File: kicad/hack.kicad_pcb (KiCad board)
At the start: 2 copper layers, 33.5 x 23.4 mm, 33 parts, among them P1 USB_micro, P2 CONN_01X13, P3 CONN_01X13, P4 CONN_01X01, U1 MIC5528, U2 STF202, U3 ATSAMD21E, X1 MC-306

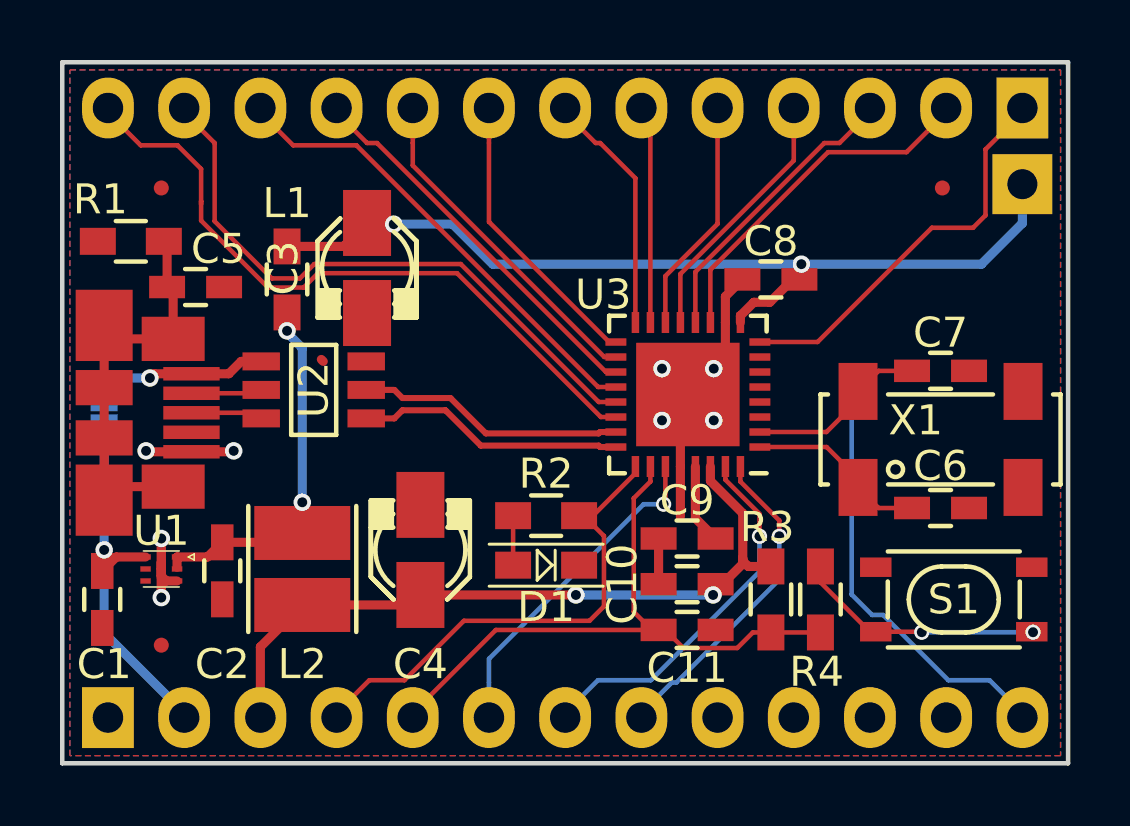
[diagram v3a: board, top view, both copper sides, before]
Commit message: Layout 100% completed, cosmetics not yet
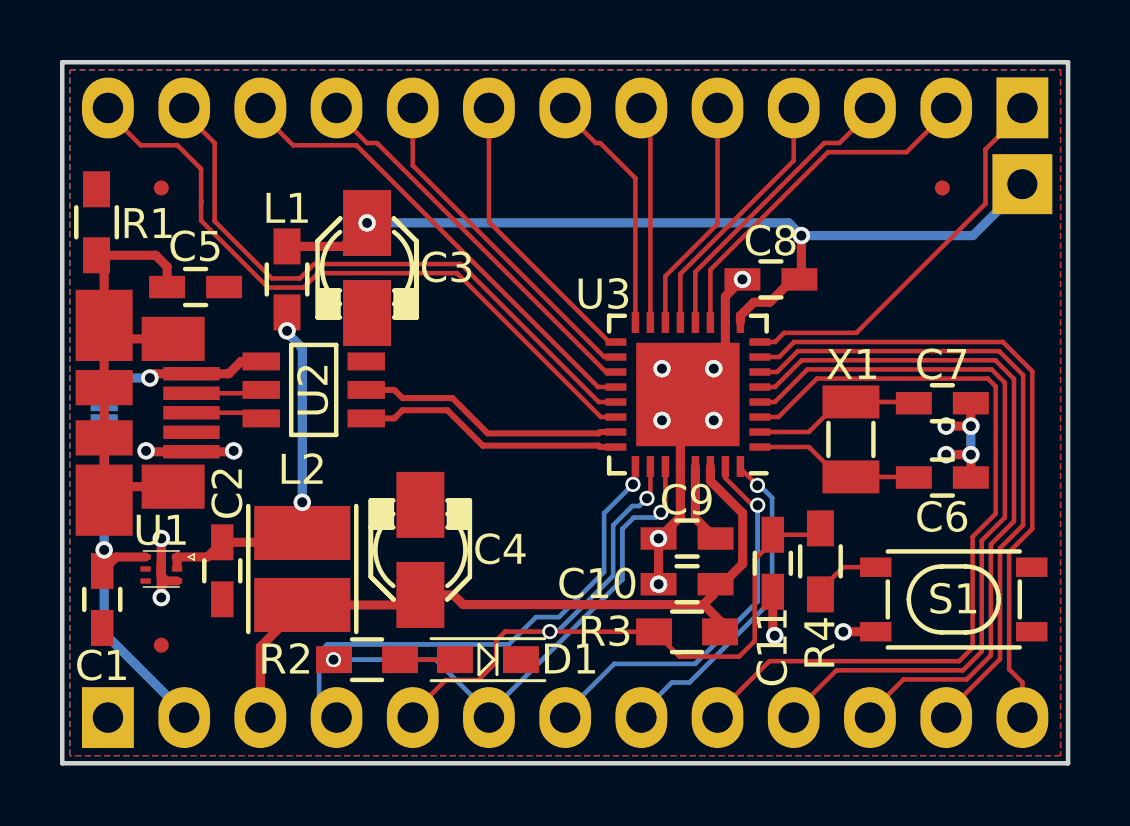
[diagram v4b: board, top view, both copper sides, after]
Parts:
- added LOGO3: HACK, hack-footprints:HACK-LOGO, B.Cu at (170.9, 84.6)
- C6, C7: value 15p -> 10p
- S1: footprint hack-footprints:SPST -> hack-footprints:SPST-PTS_810
- X1: value MC-306 -> ABS07; footprint hack-footprints:MC-306 -> hack-footprints:xtal_3.2x1.5mm
- moved R2 7.66 mm to (163.6, 94.6), turned to 0 degrees
- moved LOGO1 4.07 mm to (160.3, 90.7)
- moved D1 3.70 mm to (167.6, 94.6)
- moved C11 3.62 mm to (177.1, 91.4), turned to 270 degrees
- moved R3 3.00 mm to (174.2, 93.7), turned to 0 degrees
- moved X1 2.99 mm to (179.7, 87.2), turned to 180 degrees
- moved R1 1.31 mm to (154.6, 80.0), turned to 270 degrees
- moved R4 1.27 mm to (178.7, 91.3), turned to 270 degrees
- moved C7 1.08 mm to (182.8, 86.0)
- moved C6 1.02 mm to (182.8, 88.5)
- moved LOGO2 0.72 mm to (181.6, 90.9)
- turned S1 to 90 degrees
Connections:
- P2 pad 10: !RESET -> PA03/A1
- P2 pad 11: PA28 -> PA04/A2
- P2 pad 12: PA30/SWCLK -> PA05/A3
- P2 pad 13: PA31/SWDIO -> PA06/A4
- P2 pad 4: PA17 -> PA27/12
- P2 pad 5: PA18 -> !RESET
- P2 pad 6: PA19 -> PA28/13
- P2 pad 7: PA22 -> PA30/SWCLK
- P2 pad 8: PA23 -> PA31/SWDIO
- P2 pad 9: PA27 -> PA02/A0
- P3 pad 1: PA02/A -> PA07/A5
- P3 pad 10: PA11 -> PA18/8
- P3 pad 11: PA14 -> PA19/9
- P3 pad 12: PA15 -> PA22/10
- P3 pad 13: PA16 -> PA23/11
- P3 pad 2: PA03/A -> PA08/0
- P3 pad 3: PA04/A -> PA09/1
- P3 pad 4: PA05/A -> PA10/2
- P3 pad 5: PA06/A -> PA11/3
- P3 pad 6: PA07/A -> PA14/4
- P3 pad 7: PA08 -> PA15/5
- P3 pad 8: PA09 -> PA16/6
- P3 pad 9: PA10 -> PA17/7
- R2 pad 1: PA27 -> PA28/13
- S1 pad 2: Net-(R4-Pad2) -> Net-(S1-Pad2)
- U3 pad 11: PA08 -> PA08/0
- U3 pad 12: PA09 -> PA09/1
- U3 pad 13: PA10 -> PA10/2
- U3 pad 14: PA11 -> PA11/3
- U3 pad 15: PA14 -> PA14/4
- U3 pad 16: PA15 -> PA15/5
- U3 pad 17: PA16 -> PA16/6
- U3 pad 18: PA17 -> PA17/7
- U3 pad 19: PA18 -> PA18/8
- U3 pad 20: PA19 -> PA19/9
- U3 pad 21: PA22 -> PA22/10
- U3 pad 22: PA23 -> PA23/11
- U3 pad 25: PA27 -> PA27/12
- U3 pad 27: PA28 -> PA28/13
- U3 pad 3: PA02/A -> PA02/A0
- U3 pad 4: PA03/A -> PA03/A1
- U3 pad 5: PA04/A -> PA04/A2
- U3 pad 6: PA05/A -> PA05/A3
- U3 pad 7: PA06/A -> PA06/A4
- U3 pad 8: PA07/A -> PA07/A5
- X1 pad 2: Net-(X1-Pad2) -> XOUT32
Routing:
- net PA02/A0: track 0.00 -> 27.1 mm
- net PA03/A1: track 0.00 -> 25.3 mm
- net PA15: track 24.7 -> 0.00 mm
- net PA23: track 24.2 -> 0.00 mm, vias 1 -> 0
- net PA04/A2: track 0.00 -> 23.6 mm
- net PA23/11: track 0.00 -> 22.8 mm
- net PA05/A3: track 0.00 -> 21.9 mm
- net PA06/A4: track 0.00 -> 21.7 mm
- net PA22/10: track 0.00 -> 20.5 mm
- net PA27/12: track 0.00 -> 17.2 mm, vias 0 -> 1
- net PA28/13: track 0.00 -> 17.2 mm, vias 0 -> 2
- net PA19/9: track 0.00 -> 15.8 mm
- net PA18: track 15.3 -> 0.00 mm
- net PA14: track 15.2 -> 0.00 mm
- net PA16: track 14.9 -> 0.00 mm
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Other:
- board text added: "Design by Michele Perla"
